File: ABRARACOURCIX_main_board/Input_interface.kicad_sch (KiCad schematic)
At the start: 6 parts, among them J1 Conn_01x05_Socket, J2 Conn_01x06_Socket

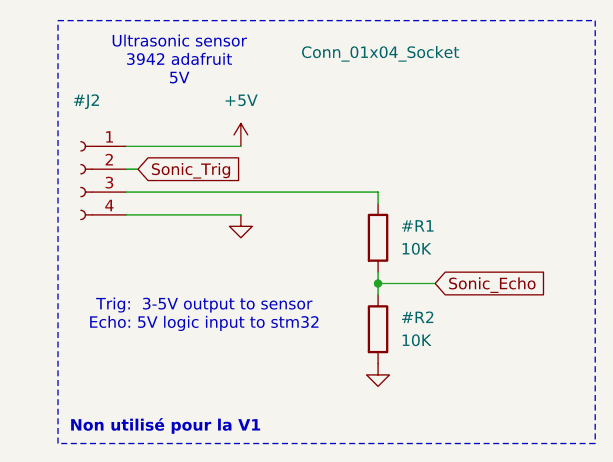
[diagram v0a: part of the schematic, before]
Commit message: Documentation, lien digikey et part number assigné à toutes les composantes
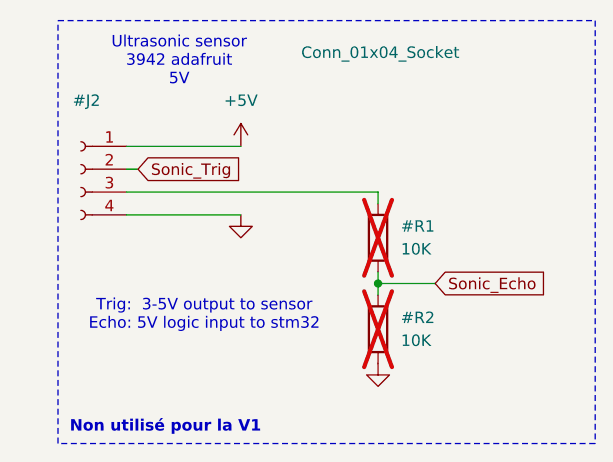
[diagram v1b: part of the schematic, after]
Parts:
- #R1, #R2: now not fitted; now left out of the parts list
- J1: Digikey (none) -> https://www.digikey.ca/en/products/detail/sullins-connector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; Part number (none) -> S5480-ND
- J2: Digikey (none) -> https://www.digikey.ca/en/products/detail/samtec-inc/SSW-10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; Part number (none) -> SSW-106-03-F-S-RA-ND
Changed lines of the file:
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@@
 		(at 69.85 140.97 0)
 		(unit 1)
-		(exclude_from_sim no)
-		(in_bom yes)
-		(on_board yes)
-		(dnp no)
+		(exclude_from_sim yes)
+		(in_bom no)
+		(on_board no)
+		(dnp yes)
 		(fields_autoplaced yes)
 		(property "Reference" "#R1"
@@
 		)
 		(property "Description" "Resistor"
+			(at 69.85 140.97 0)
+			(effects
+				(font
+					(size 1.27 1.27)
+				)
+				(hide yes)
+			)
+		)
+		(property "Digikey" ""
+			(at 69.85 140.97 0)
+			(effects
+				(font
+					(size 1.27 1.27)
+				)
+				(hide yes)
+			)
+		)
+		(property "Part number" ""
 			(at 69.85 140.97 0)
 			(effects
@@
 			)
 		)
-		(property "Datasheet" "~"
+		(property "Datasheet" "https://mm.digikey.com/Volume0/opasdata/d220001/medias/docus/937/Female_Headers.100_DS.pdf"
 			(at 55.88 35.56 0)
 			(effects
@@
 			)
 		)
-		(property "Description" ""
+		(property "Description" "CONN HDR 5POS 0.1 GOLD PCB R/A"
 			(at 55.88 35.56 0)
 			(effects
@@
 			)
 		)
-		(property "Digikey" ""
+		(property "Digikey" "https://www.digikey.ca/en/products/detail/sullins-connector-solutions/PPPC051LGBN-RC/775938"
+			(at 55.88 35.56 0)
+			(effects
+				(font
+					(size 1.27 1.27)
+				)
+				(hide yes)
+			)
+		)
+		(property "Part number" "S5480-ND"
 			(at 55.88 35.56 0)
 			(effects
@@
 			)
 		)
-		(property "Datasheet" "~"
+		(property "Datasheet" "https://mm.digikey.com/Volume0/opasdata/d220001/medias/docus/6129/ssw-1xx-xx-xxx-x-xx-xxx-xx-mkt.pdf"
 			(at 53.34 102.87 0)
 			(effects
@@
 		)
 		(property "Description" "Generic connector, single row, 01x06, script generated"
+			(at 53.34 102.87 0)
+			(effects
+				(font
+					(size 1.27 1.27)
+				)
+				(hide yes)
+			)
+		)
+		(property "Digikey" "https://www.digikey.ca/en/products/detail/samtec-inc/SSW-106-03-F-S-RA/7893166"
+			(at 53.34 102.87 0)
+			(effects
+				(font
+					(size 1.27 1.27)
+				)
+				(hide yes)
+			)
+		)
+		(property "Part number" "SSW-106-03-F-S-RA-ND"
 			(at 53.34 102.87 0)
 			(effects
@@
 		(unit 1)
 		(exclude_from_sim no)
-		(in_bom yes)
-		(on_board yes)
-		(dnp no)
+		(in_bom no)
+		(on_board no)
+		(dnp yes)
 		(fields_autoplaced yes)
 		(property "Reference" "#R2"
@@
 			(at 69.85 151.13 0)
 			(effects
+				(font
+					(size 1.27 1.27)
+				)
+				(hide yes)
+			)
+		)
+		(property "Digikey" ""
+			(at 69.85 151.13 0)
+			(effects
+				(font
+					(size 1.27 1.27)
+				)
+				(hide yes)
+			)
+		)
+		(property "Part number" ""
+			(at 69.85 151.13 0)
+			(effects
